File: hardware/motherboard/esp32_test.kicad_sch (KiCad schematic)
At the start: 17 parts, among them J2 USB C 2.0, Q1 TSM7P06CP_ROG, U1 ESP32-S3-WROOM-1, U2 TPS75533KTTRG3

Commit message: Basic Microcontroller Stuff and Display Power
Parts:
- added C10, C7, C9: 1uF, symbol Device:C
- added C8: 10uF, symbol Device:C
- added D2: LED1, symbol Device:LED
- added D3: LED2, symbol Device:LED
- added J1: JST-PH, symbol Connector_Generic:Conn_01x02
- added J3: JST-VH, symbol Connector_Generic:Conn_01x02
- added J4: JST-PH, symbol Connector_Generic:Conn_01x08
- added Q2: TSM7P06CP_ROG, TSM7P06CPROG, symbol Library_Loader:TSM7P06CP_ROG
- added R10, R9: 100, symbol Device:R_US
- added R5, R6: 1M, symbol Device:R_US
- added R7, R8: 10k, symbol Device:R_US
- added SW1: Boot, symbol Switch:SW_Push
- added SW2: Reset, symbol Switch:SW_Push
- added TP3: 3V3, symbol Connector:TestPoint
- added TP4: GND, symbol Connector:TestPoint
- added TP5: VBat, symbol Connector:TestPoint
- added TP6: ABat, symbol Connector:TestPoint
- added U3: TLV75709PDBV, Package_TO_SOT_SMD:SOT-23-5, symbol Regulator_Linear:TLV75709PDBV
- C2: value 1uF -> 0.1uF
- TP1: value VLDO -> VIN
- TP2: value 3V3 -> VDisplay
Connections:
- net +3V3: now also U1.2 (3V3), C8.1, R7.2, R8.2, TP3.1, U3.5 (OUT); no longer C3.1, R2.2, TP2.1, U2.4 (OUT)
- net D+: now also U1.14 (USB_D+)
- net D-: now also U1.13 (USB_D-)
- net GND: now also U1.1 (GND), U1.40 (GND), U1.41 (GND), C10.2, C7.2, C8.2, C9.2, J1.1 (Pin_1), J3.2 (Pin_2), Q2.1 (G), R10.1, R6.2, R9.1, SW1.2, SW2.2, TP4.1, U3.2 (GND)
- net VBat: now also Q2.3 (S), R5.1, TP5.1
- net VIN: now reaches D1.4, Q1.3 (S), TP1.1, U2.2 (IN)
- net VIN: now also C7.1, U3.1 (IN), U3.3 (EN); no longer C2.1
- net Boot: now reaches U1.27 (IO0)
- net Boot: now also C9.1, R7.1, SW1.1
- net En: now reaches U1.3 (EN)
- net En: now also C10.1, R8.1, SW2.1
- net LED1: now reaches U1.33 (IO40)
- net LED1: now also D2.2 (A)
- net LED2: now reaches U1.35 (IO42)
- net LED2: now also D3.2 (A)
- new net: J1.2 (Pin_2), Q2.2 (D)
- new net: D2.1 (K), R9.2
- new net: D3.1 (K), R10.2
- new net ABat: C2.1, R5.2, R6.1, TP6.1
- new net Dis1: J4.1 (Pin_1)
- new net Dis2: J4.2 (Pin_2)
- new net Dis3: J4.3 (Pin_3)
- new net Dis4: J4.4 (Pin_4)
- new net Dis5: J4.5 (Pin_5)
- new net Dis6: J4.6 (Pin_6)
- new net Dis7: J4.7 (Pin_7)
- new net Dis8: J4.8 (Pin_8)
- new net VDisplay: C3.1, J3.1 (Pin_1), R2.2, TP2.1, U2.4 (OUT)
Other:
- note added: "(to ADC)"
- note added: "1S LiIon Connector"
- note added: "Battery Charger"
- note added: "Display Connectors"
- note added: "Display Power Regulator"
- note added: "LDO, Bulk Caps"
- note added: "LEDs"
- note added: "Source Select"
- note added: "TODO: Select Battery Charger IC"
- note added: "Tech Buttons"
- note added: "Voltage Divider"
- note removed: "Source Select, Bulk Caps, LDO"
- company: (none) -> "Gamers"
- title: (none) -> Handheld Game Motherboard
- moved on the sheet: C1, C3, C4, C5, C6, D1, J2, Q1, R1, R2, R3, R4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

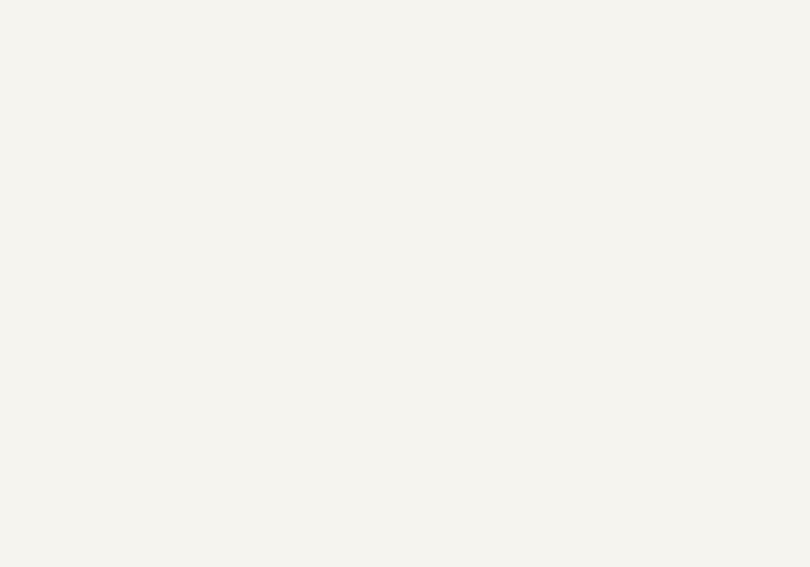
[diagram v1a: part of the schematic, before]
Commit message: Changed GitIgnore
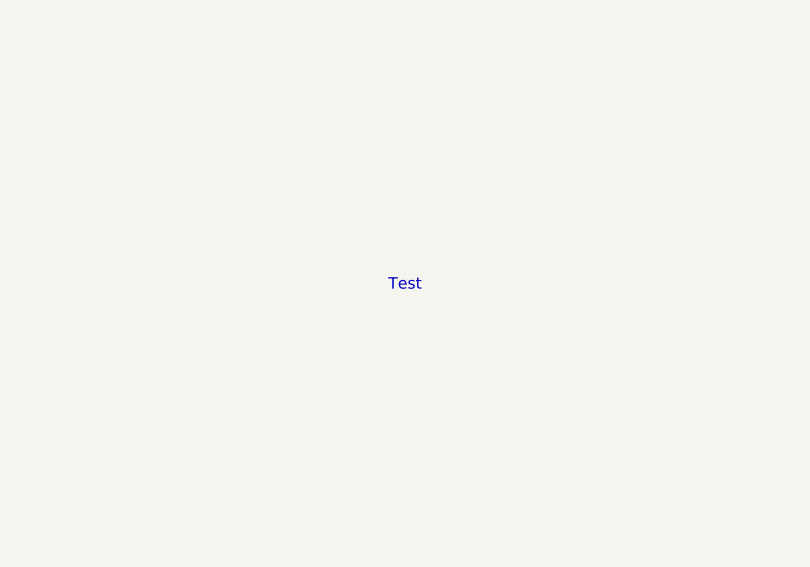
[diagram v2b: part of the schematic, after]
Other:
- note added: "Test"
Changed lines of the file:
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@@
+		)
+	)
+	(text "Test"
+		(exclude_from_sim no)
+		(at 75.438 80.772 0)
+		(effects
+			(font
+				(size 1.27 1.27)
+			)
 		)
 	)

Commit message: Updated GitIgnore
Changed Gitignore to ignore backup generation
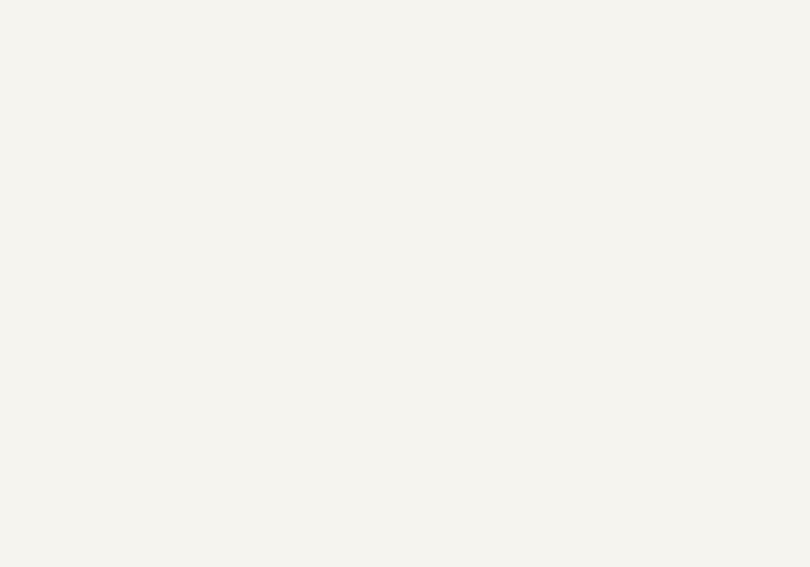
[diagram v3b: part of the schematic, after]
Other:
- note removed: "Test"
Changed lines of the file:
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@@
-		)
-	)
-	(text "Test"
-		(exclude_from_sim no)
-		(at 75.438 80.772 0)
-		(effects
-			(font
-				(size 1.27 1.27)
-			)
 		)
 	)

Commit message: Fixed Capacitors
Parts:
- removed C6: 10uF, symbol Device:C_Small
- removed C8: 10uF, symbol Device:C
- added C11, C6: 10uF, symbol Device:C_Polarized_Small_US
- J1: value JST-PH -> JST-VH
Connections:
- net +3V3: now also C11.1, C6.1
- net GND: now also C11.2, C6.2
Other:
- note added: "Confirm ESR of capacitor! Must be above 500m"
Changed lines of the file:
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@@
 		)
 	)
+	(text "Confirm ESR\nof capacitor!\nMust be above \n500m"
+		(exclude_from_sim no)
+		(at 226.822 160.274 0)
+		(effects
+			(font
+				(size 0.635 0.635)
+				(thickness 0.127)
+				(bold yes)
+			)
+			(justify left)
+		)
+	)
 	(text "Battery Charger"
 		(exclude_from_sim no)
@@
 	(wire
 		(pts
-			(xy 163.83 167.64) (xy 163.83 166.37)
-		)
-		(stroke
-			(width 0)
-			(type default)
-		)
-	)
-	(wire
-		(pts
 			(xy 247.65 146.05) (xy 248.92 146.05)
 		)
@@
 	(wire
 		(pts
+			(xy 163.83 166.37) (xy 163.83 168.91)
+		)
+		(stroke
+			(width 0)
+			(type default)
+		)
+	)
+	(wire
+		(pts
 			(xy 119.38 166.37) (xy 119.38 168.91)
 		)
@@
 	(wire
 		(pts
-			(xy 163.83 175.26) (xy 163.83 176.53)
+			(xy 163.83 173.99) (xy 163.83 176.53)
 		)
 		(stroke
@@
 	)
 	(symbol
-		(lib_id "Device:C")
-		(at 163.83 171.45 0)
-		(unit 1)
-		(exclude_from_sim no)
-		(in_bom yes)
-		(on_board yes)
-		(dnp no)
-		(property "Reference" "C8"
-			(at 158.496 170.688 0)
-			(effects
-				(font
-					(size 1.27 1.27)
-				)
-				(justify left)
-			)
-		)
-		(property "Value" "10uF"
-			(at 156.464 172.974 0)
-			(effects
-				(font
-					(size 1.27 1.27)
-				)
-				(justify left)
-			)
-		)
-		(property "Footprint" ""
-			(at 164.7952 175.26 0)
-			(effects
-				(font
-					(size 1.27 1.27)
-				)
-				(hide yes)
-			)
-		)
-		(property "Datasheet" "~"
-			(at 163.83 171.45 0)
-			(effects
-				(font
-					(size 1.27 1.27)
-				)
-				(hide yes)
-			)
-		)
-		(property "Description" "Unpolarized capacitor"
-			(at 163.83 171.45 0)
-			(effects
-				(font
-					(size 1.27 1.27)
-				)
-				(hide yes)
-			)
-		)
-		(pin "1"
-		)
-		(pin "2"
-		)
-		(instances
-			(project "esp32_test"
-				(path "/4bd92664-563a-4440-acf2-e22b0a15db62"
-					(reference "C8")
-					(unit 1)
-				)
-			)
-		)
-	)
-	(symbol
 		(lib_id "power:GND")
 		(at 146.05 146.05 0)
@@
 	)
 	(symbol
+		(lib_id "Device:C_Polarized_Small_US")
+		(at 163.83 171.45 0)
+		(unit 1)
+		(exclude_from_sim no)
+		(in_bom yes)
+		(on_board yes)
+		(dnp no)
+		(fields_autoplaced yes)
+		(property "Reference" "C6"
+			(at 166.37 169.7481 0)
+			(effects
+				(font
+					(size 1.27 1.27)
+				)
+				(justify left)
+			)
+		)
+		(property "Value" "10uF"
+			(at 166.37 172.2881 0)
+			(effects
+				(font
+					(size 1.27 1.27)
+				)
+				(justify left)
+			)
+		)
+		(property "Footprint" ""
+			(at 163.83 171.45 0)
+			(effects
+				(font
+					(size 1.27 1.27)
+				)
+				(hide yes)
+			)
+		)
+		(property "Datasheet" "~"
+			(at 163.83 171.45 0)
+			(effects
+				(font
+					(size 1.27 1.27)
+				)
+				(hide yes)
+			)
+		)
+		(property "Description" "Polarized capacitor, small US symbol"
+			(at 163.83 171.45 0)
+			(effects
+				(font
+					(size 1.27 1.27)
+				)
+				(hide yes)
+			)
+		)
+		(pin "2"
+		)
+		(pin "1"
+		)
+		(instances
+			(project "esp32_test"
+				(path "/4bd92664-563a-4440-acf2-e22b0a15db62"
+					(reference "C6")
+					(unit 1)
+				)
+			)
+		)
+	)
+	(symbol
+		(lib_id "Device:C_Polarized_Small_US")
+		(at 158.75 190.5 0)
+		(unit 1)
+		(exclude_from_sim no)
+		(in_bom yes)
+		(on_board yes)
+		(dnp no)
+		(fields_autoplaced yes)
+		(property "Reference" "C11"
+			(at 161.29 188.7981 0)
+			(effects
+				(font
+					(size 1.27 1.27)
+				)
+				(justify left)
+			)
+		)
+		(property "Value" "10uF"
+			(at 161.29 191.3381 0)
+			(effects
+				(font
+					(size 1.27 1.27)
+				)
+				(justify left)
+			)
+		)
+		(property "Footprint" ""
+			(at 158.75 190.5 0)
+			(effects
+				(font
+					(size 1.27 1.27)
+				)
+				(hide yes)
+			)
+		)
+		(property "Datasheet" "~"
+			(at 158.75 190.5 0)
+			(effects
+				(font
+					(size 1.27 1.27)
+				)
+				(hide yes)
+			)
+		)
+		(property "Description" "Polarized capacitor, small US symbol"
+			(at 158.75 190.5 0)
+			(effects
+				(font
+					(size 1.27 1.27)
+				)
+				(hide yes)
+			)
+		)
+		(pin "2"
+		)
+		(pin "1"
+		)
+		(instances
+			(project ""
+				(path "/4bd92664-563a-4440-acf2-e22b0a15db62"
+					(reference "C11")
+					(unit 1)
+				)
+			)
+		)
+	)
+	(symbol
 		(lib_id "Connector:TestPoint")
 		(at 17.78 139.7 270)
@@
 			)
 		)
-		(property "Value" "JST-PH"
+		(property "Value" "JST-VH"
 			(at 22.86 123.444 90)
 			(effects
@@
 					(unit 1)
 				)
-			)
-		)
-	)
-	(symbol
-		(lib_id "Device:C_Small")
-		(at 158.75 190.5 0)
-		(unit 1)
-		(exclude_from_sim no)
-		(in_bom yes)
-		(on_board yes)
-		(dnp no)
-		(fields_autoplaced yes)
-		(property "Reference" "C6"
-			(at 161.29 189.2362 0)
-			(effects
-				(font
-					(size 1.27 1.27)
-				)
-				(justify left)
-			)
-		)
-		(property "Value" "10uF"
-			(at 161.29 191.7762 0)
-			(effects
-				(font
-					(size 1.27 1.27)
-				)
-				(justify left)
-			)
-		)
-		(property "Footprint" ""
-			(at 158.75 190.5 0)
-			(effects
-				(font
-					(size 1.27 1.27)
-				)
-				(hide yes)
-			)
-		)
-		(property "Datasheet" "~"
-			(at 158.75 190.5 0)
-			(effects
-				(font
-					(size 1.27 1.27)
-				)
-				(hide yes)
-			)
-		)
-		(property "Description" "Unpolarized capacitor, small symbol"
-			(at 158.75 190.5 0)
-			(effects
-				(font
-					(size 1.27 1.27)
-				)
-				(hide yes)
-			)
-		)
-		(pin "1"
-		)
-		(pin "2"
-		)
-		(instances
-			(project "esp32_test"
-				(path "/4bd92664-563a-4440-acf2-e22b0a15db62"
-					(reference "C6")
-					(unit 1)
-				)
